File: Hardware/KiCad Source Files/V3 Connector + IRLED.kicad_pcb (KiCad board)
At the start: 2 copper layers, 60 x 126.6 mm, 151 parts, among them J1 YK3210203000G, J2 USB4085-GF-A, J3 Conn_01x08, J4 YK3210203000G, J5 USB4085-GF-A, J6 USB1125-GF-B, Q1 IRLU024NPBF, Q2 IRLU024NPBF, Q3 Q_NMOS, U1 MC33063AP, U4 LM4040LP-2.0, U5 MCP4801, U6 MCP3202

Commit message: V3 connector board: strobe pulse limiter, USB-C fixes, boost protection
Mechanical: board outline, all mounting/tab/breakaway holes and every
existing part position are unchanged (checked against the previous revision);
all new parts are on the top side and no taller than existing parts.
PiTrac software compatibility: the LED current-control circuit and the
DAC/ADC/DIAG interface used by strobe_calibration_manager.py are unchanged.

Strobe (CC Sink sheet)
- AC-coupled pulse limiter: TRIG (DIAG/MOSI via D3/D4) -> C16 220nF ->
  GATE-DRV, R28 10K to GND (tau 2.2 ms). 8.7-130 us strobes and the
  calibration pulse pass (guaranteed >= ~0.38 ms by the MCP1407 input
  limits); a stuck-high DIAG turns the driver off after ~1.7 ms typical,
  <= ~2.8 ms worst case, so 10 A can no longer be held on.

USB-C (Connectors sheet, USB4085-GF-A footprint)
- J2/J5 feed 5 V to the Pis: add 10K Rp on CC1/CC2 (R24-R27, 1206).
- Footprint rebuilt to GCT's land pattern (16 plated 0.40/0.66 mm pins).
  The old VBUS/GND pads had 0.1 mm top-side copper (annular-ring DRC
  errors; Pi supply current only reached them via the barrel/bottom pad).

Boost (Power sheet)
- F1 MF-MSMF050-2 polyfuse in the boost input only (+5V_BST: C1/C2/C3/R1/
  U1); PCB: +5V_BST F.Cu island, +5V B.Cu bridge keeps the Pi feed width.
- D16 P4SMA39CA clamp on VIR (open-feedback fault; relies on F1).
- R5 2K49 -> 10K (was ~0.45 W in a 1/4 W resistor).

Housekeeping
- Project sym/fp-lib-tables; USB4085-GF-A added to the symbol library;
  pin types for custom parts; locally modified Q_NPN/Q_NMOS/LED moved into
  the project library (Q_NPN_EBC, Q_NMOS_SGD, LED_ThermalPad) to keep their
  numeric pinouts; no-connect flags; PWR_FLAGs; GATE-DRV wire to Q3 fixed.
- ERC pin map (project-wide): open emitter on a power rail allowed
  (MC33063 SwE to GND).
- Add V3 Connector Only.kicad_pro (board had no rules; DRC used defaults).
- Breakaway holes marked board-only.
- Regenerated Gerber/drill zips, BOM and centroid CSVs (same for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
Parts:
- added C16: 220nF, Capacitor_THT:C_Disc_D4.3mm_W1.9mm_P5.00mm, F.Cu at (114.0, 132.5)
- added D16: P4SMA39CA, Diode_SMD:D_SMA, F.Cu at (101.8, 93.0)
- added F1: 0.5A hold, Fuse:Fuse_1812_4532Metric_Pad1.30x3.40mm_HandSolder, F.Cu at (62.5, 105.2)
- added R24: 10K, Resistor_SMD:R_1206_3216Metric_Pad1.30x1.75mm_HandSolder, F.Cu at (69.0, 126.6)
- added R25: 10K, Resistor_SMD:R_1206_3216Metric_Pad1.30x1.75mm_HandSolder, F.Cu at (63.5, 126.6)
- added R26: 10K, Resistor_SMD:R_1206_3216Metric_Pad1.30x1.75mm_HandSolder, F.Cu at (68.0, 143.3)
- added R27: 10K, Resistor_SMD:R_1206_3216Metric_Pad1.30x1.75mm_HandSolder, F.Cu at (63.0, 143.3)
- added R28: 10K, Resistor_THT:R_Axial_DIN0207_L6.3mm_D2.5mm_P2.54mm_Vertical, F.Cu at (117.5, 130.0)
- R5: value 2K49 -> 10K
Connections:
- C1 pad 1: +5V -> +5V_BST
- C2 pad 1: +5V -> +5V_BST
- C3 pad 1: +5V -> +5V_BST
- D3 pad 1: /CC Sink/GATE-DRV -> /CC Sink/TRIG
- D4 pad 1: /CC Sink/GATE-DRV -> /CC Sink/TRIG
- R1 pad 2: +5V -> +5V_BST
- R8 pad 2: /CC Sink/GATE-DRV -> /CC Sink/TRIG
- U1 pad 6: +5V -> +5V_BST
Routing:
- net +5V_BST: track 0.00 -> 22.8 mm
- net +5V: track 18.9 -> 0.00 mm, vias 0 -> 9
- net /CC Sink/TRIG: track 0.00 -> 16.3 mm
- net /Connectors/J5_CC1: track 0.00 -> 11.0 mm
- net /Connectors/J2_CC1: track 0.00 -> 10.9 mm
- net /Connectors/J5_CC2: track 0.00 -> 8.77 mm
- net /Connectors/J2_CC2: track 0.00 -> 8.68 mm
- net VIR: track 70.5 -> 72.6 mm
- net /CC Sink/GATE-DRV: track 25.5 -> 27.2 mm, vias 0 -> 1
- net GND: vias 500 -> 486
- added copper zone on B.Cu, net +5V
- added copper zone on F.Cu, net +5V_BST

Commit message: C16: use an orderable part (K224K20X7RF5UH5, 220nF 50V X7R)
K224K15X7RF5UH5 isn't listed by any distributor; the "20" (50 V) code is the
real 220 nF part in this Vishay K series (DigiKey 2356767, element14
2860121). Footprint moved to C_Disc_D5.1mm_W3.2mm_P5.00mm, the one already
used for C2 (1 uF in the same series), so the body fits.
Outputs regenerated; ERC/DRC unchanged (0 errors), geometry unchanged.

Co-Authored-By: Claude Opus 5.5 <noreply@anthropic.com>
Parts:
- C16: footprint Capacitor_THT:C_Disc_D4.3mm_W1.9mm_P5.00mm -> Capacitor_THT:C_Disc_D5.1mm_W3.2mm_P5.00mm

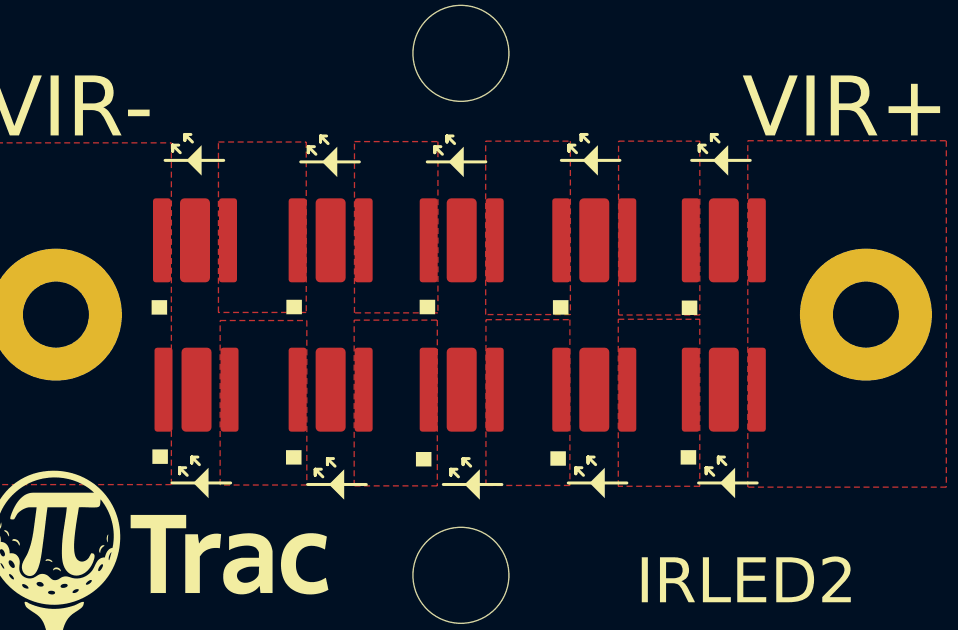
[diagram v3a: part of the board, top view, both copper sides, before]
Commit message: IR LEDs: connect the VSMA1085400 center pad (second anode) on both LED boards
Vishay's package drawing (doc 80294) labels the VSMA1085400 pads Anode,
Anode, Cathode; the wide center pad under the die is an anode contact, not
an isolated thermal pad. The LED symbol was inherited from the earlier
Luminus SST-10-IRD (whose center pad is isolated), so pad 3 was left on an
isolated copper island and all strobe current went through the 0.35 mm
outer anode pad.

- Symbol: LED_ThermalPad -> VSMA1085400 (pin 3 named A, Vishay datasheet,
  description). D6-D15 pin 3 wired to pin 2; no-connect markers removed.
- PCB (IRLED Only, and the LED tab of V3 Connector + IRLED): pad 3 on the
  LED's anode net with a 2 mm bridge to pad 2. The gap to the cathode pad
  stays 0.3 mm. LED positions, holes and outline unchanged.
- Two anode nets were auto-renamed by the schematic (Net-(D11-A) ->
  Net-(D11-A-Pad2), Net-(D10-A) -> Net-(D9-K)); pours/pads renamed to match.
- Regenerated IRLED2 Only and V3 Connector + IRLED2 Gerbers and the
  schematic PDF (BOM/centroid unchanged).

ERC 0 (1 intended exclusion). DRC all three boards: 0 errors.

Co-Authored-By: Claude Opus 5.5 <noreply@anthropic.com>
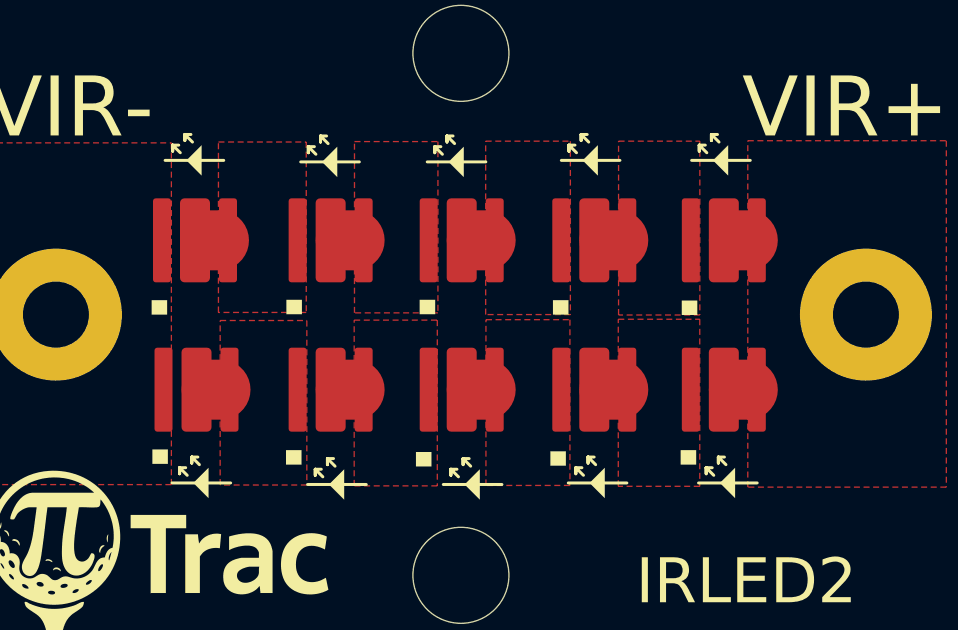
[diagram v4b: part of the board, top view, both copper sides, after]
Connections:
- D10 pad 2: Net-(D10-A) -> Net-(D9-K)
- D10 pad 3: unconnected-(D10-P-Pad3) -> Net-(D9-K)
- D11 pad 2: Net-(D11-A) -> Net-(D11-A-Pad2)
- D11 pad 3: unconnected-(D11-P-Pad3) -> Net-(D11-A-Pad2)
- D12 pad 3: unconnected-(D12-P-Pad3) -> Net-(D11-K)
- D13 pad 3: unconnected-(D13-P-Pad3) -> Net-(D12-K)
- D14 pad 3: unconnected-(D14-P-Pad3) -> Net-(D13-K)
- D15 pad 3: unconnected-(D15-P-Pad3) -> Net-(D14-K)
- D6 pad 2: Net-(D11-A) -> Net-(D11-A-Pad2)
- D6 pad 3: unconnected-(D6-P-Pad3) -> Net-(D11-A-Pad2)
- D7 pad 3: unconnected-(D7-P-Pad3) -> Net-(D6-K)
- D8 pad 3: unconnected-(D8-P-Pad3) -> Net-(D7-K)
- D9 pad 1: Net-(D10-A) -> Net-(D9-K)
- D9 pad 3: unconnected-(D9-P-Pad3) -> Net-(D8-K)
- H5 pad 1: Net-(D11-A) -> Net-(D11-A-Pad2)
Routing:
- net Net-(D11-A-Pad2): track 0.00 -> 0.60 mm
- added copper zone on F.Cu, net Net-(D11-A-Pad2)
- added copper zone on F.Cu, net Net-(D9-K)
- removed copper zone on F.Cu, net Net-(D10-A)
- removed copper zone on F.Cu, net Net-(D11-A)
